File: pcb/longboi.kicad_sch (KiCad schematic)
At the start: 25 parts, among them J1 Testpad, J2 Testpad, J3 Testpad, J4 Testpad, J5 Testpad, J6 JST-ZH, U1 STM32H723VGTx, Y1 Crystal_GND24

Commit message: fixes #3: increased input/output capacitor values for ME6211C33M5
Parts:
- C3, C6: value 12pF -> 20pF

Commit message: fixes #8: changed led series resistor values
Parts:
- R1: value 1k -> 2.7k

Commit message: fixes #15
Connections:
- no-connect marks 10 -> 14

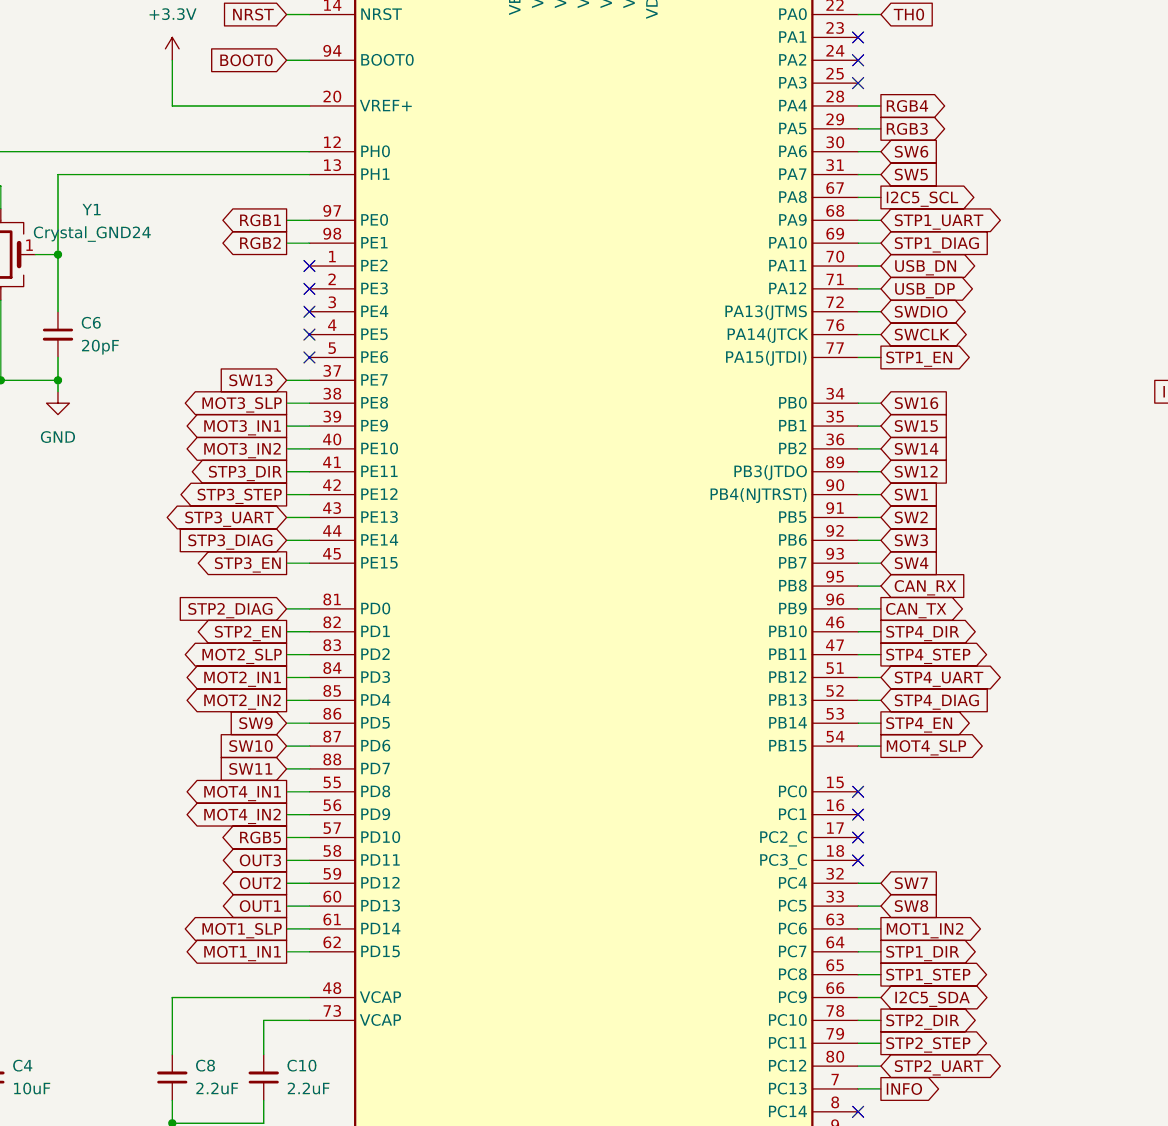
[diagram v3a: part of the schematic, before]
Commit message: fixes #7
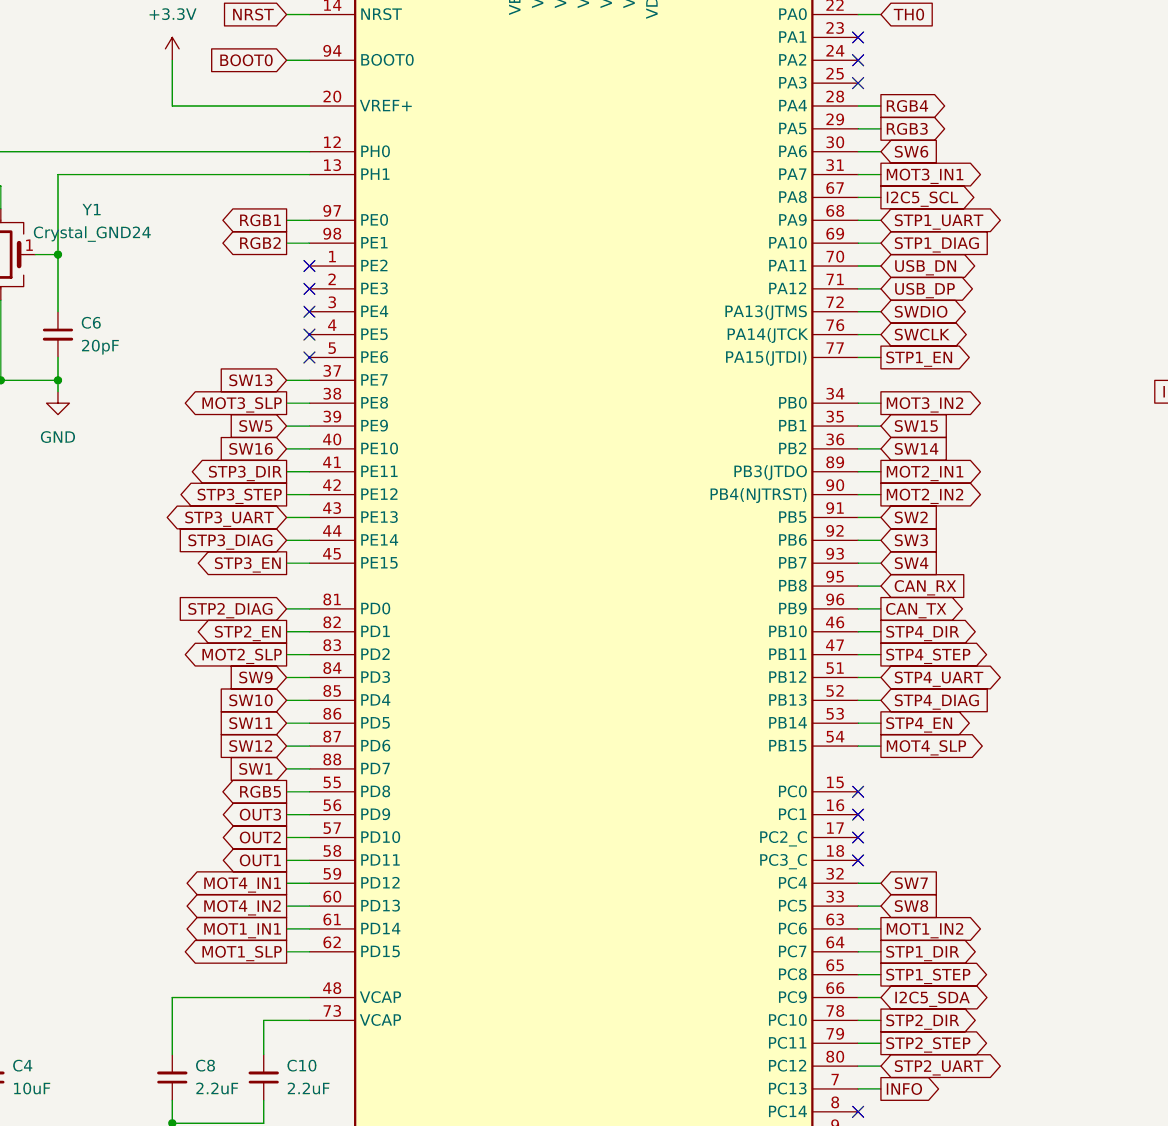
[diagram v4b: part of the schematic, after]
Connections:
- net MOT1_IN1: now also U1.61 (PD14); no longer U1.62 (PD15)
- net MOT1_SLP: now also U1.62 (PD15); no longer U1.61 (PD14)
- net MOT2_IN1: now also U1.89 (PB3(JTDO); no longer U1.84 (PD3)
- net MOT2_IN2: now also U1.90 (PB4(NJTRST)); no longer U1.85 (PD4)
- net MOT3_IN1: now also U1.31 (PA7); no longer U1.39 (PE9)
- net MOT3_IN2: now also U1.34 (PB0); no longer U1.40 (PE10)
- net MOT4_IN1: now also U1.59 (PD12); no longer U1.55 (PD8)
- net MOT4_IN2: now also U1.60 (PD13); no longer U1.56 (PD9)
- net OUT1: now also U1.58 (PD11); no longer U1.60 (PD13)
- net OUT2: now also U1.57 (PD10); no longer U1.59 (PD12)
- net OUT3: now also U1.56 (PD9); no longer U1.58 (PD11)
- net RGB5: now also U1.55 (PD8); no longer U1.57 (PD10)
- net SW1: now also U1.88 (PD7); no longer U1.90 (PB4(NJTRST))
- net SW10: now also U1.85 (PD4); no longer U1.87 (PD6)
- net SW11: now also U1.86 (PD5); no longer U1.88 (PD7)
- net SW12: now also U1.87 (PD6); no longer U1.89 (PB3(JTDO)
- net SW16: now also U1.40 (PE10); no longer U1.34 (PB0)
- net SW5: now also U1.39 (PE9); no longer U1.31 (PA7)
- net SW9: now also U1.84 (PD3); no longer U1.86 (PD5)

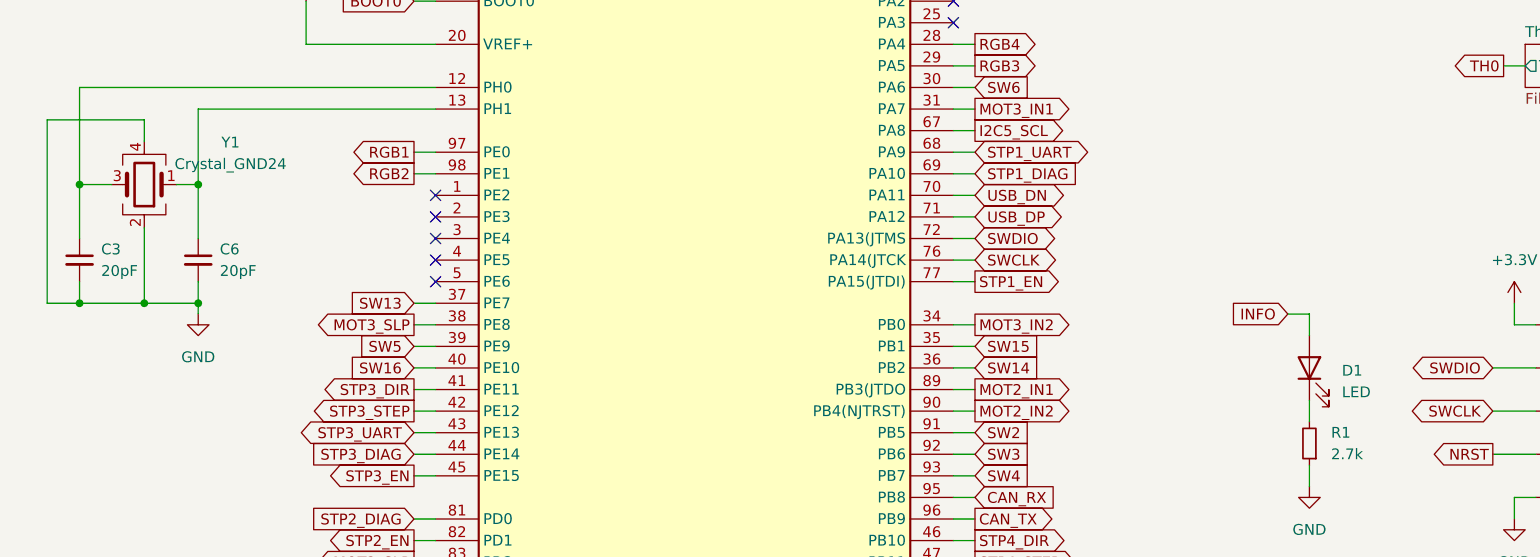
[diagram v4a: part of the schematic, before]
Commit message: specified some values and colors added lcsc part ids for all components
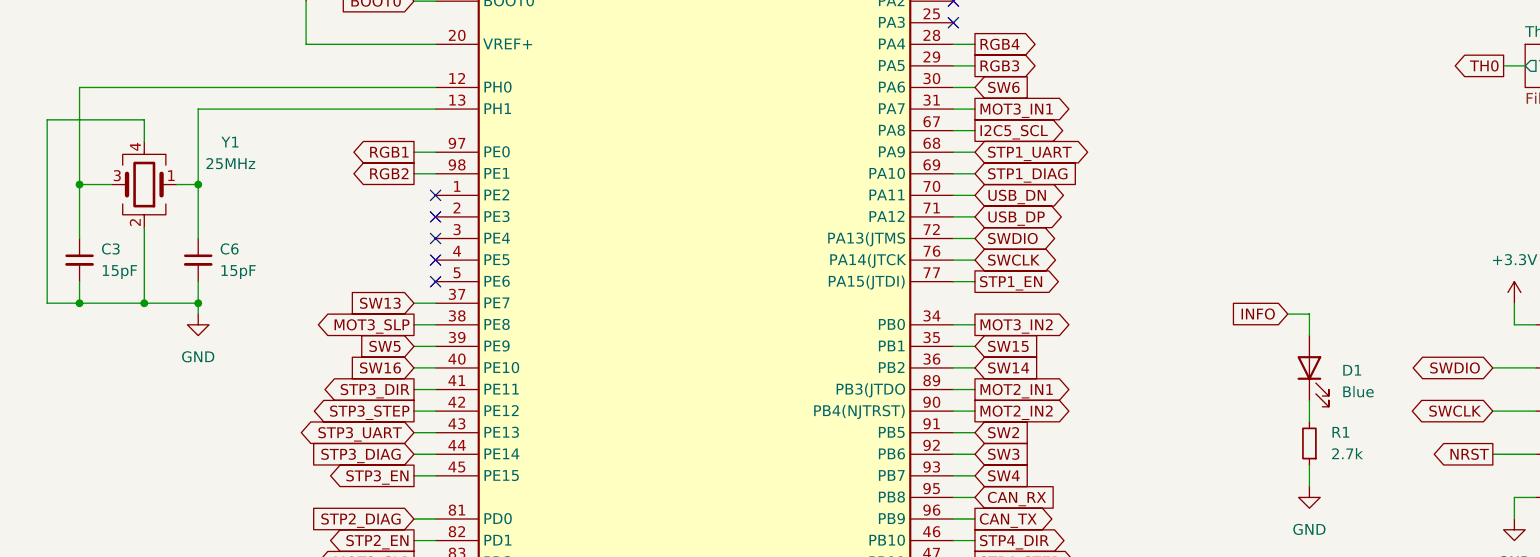
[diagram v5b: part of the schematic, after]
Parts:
- C1, C4: LCSC (none) -> C19702
- C10, C8: LCSC (none) -> C23630
- C11, C12, C13, C2, C5, C7, C9: LCSC (none) -> C14663
- C3, C6: value 20pF -> 15pF; LCSC (none) -> C1644
- D1: value LED -> Blue; LCSC (none) -> C965807
- J6: LCSC (none) -> C157997
- R1: LCSC (none) -> C13167
- R2, R3: LCSC (none) -> C22809
- U1: LCSC (none) -> C730142
- Y1: value Crystal_GND24 -> 25MHz; LCSC (none) -> C2925590

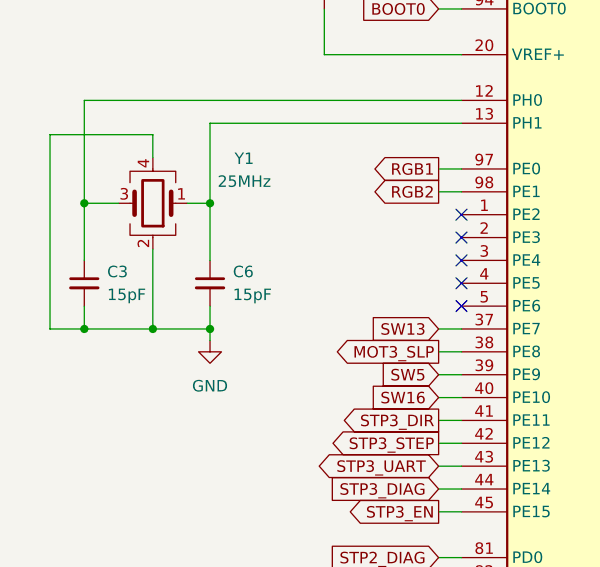
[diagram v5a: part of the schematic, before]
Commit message: fix wrong lcsc id for crystal cover up swapped net for sw3 and sw4 by swapping in config
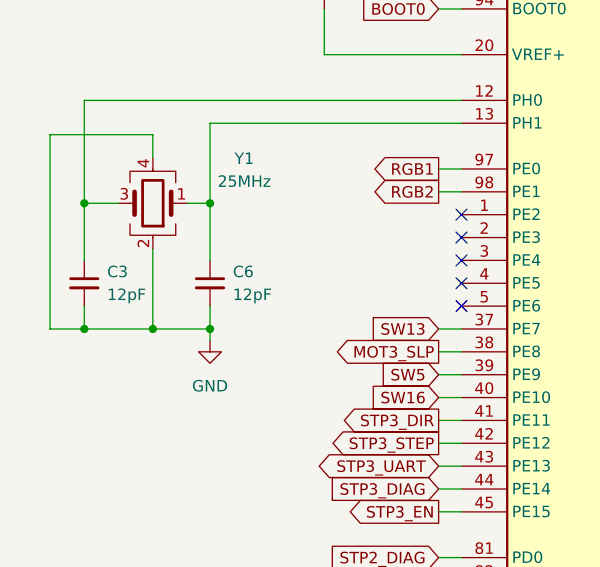
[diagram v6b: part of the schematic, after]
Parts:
- C3, C6: value 15pF -> 12pF
- Y1: LCSC C2925590 -> C9006

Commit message: fixes #20 fixes #22 fixes #19
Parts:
- J1, J2, J3, J4, J5: now left out of the parts list

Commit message: wip
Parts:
- added H1: Center, MountingHole:MountingHole_3.2mm_M3_ISO7380_Pad, symbol Mechanical:MountingHole_Pad
- added H2, H3, H4, H5, H6, H7: Slot, Longboi_Custom:MountingSlot3.2mm, symbol Mechanical:MountingHole_Pad
- J6: value JST-ZH -> JST-PH; footprint Connector_JST:JST_ZH_B4B-ZR_1x04_P1.50mm_Vertical -> Connector_JST:JST_PH_B4B-PH-K_1x04_P2.00mm_Vertical
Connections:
- net GND: now also H1.1, H2.1, H3.1, H4.1, H5.1, H6.1, H7.1
